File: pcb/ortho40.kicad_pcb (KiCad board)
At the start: 2 copper layers, 284 x 84 mm, 129 parts, among them J1 SWD, J2 USB_C_Receptacle_USB2.0, SW1 SW_Push, U1 RP2040, U2 XC6206PxxxMR, U3 W25Q128JVS, U4 USBLC6-2SC6, U5 ST7735S_1.8inch, Y1 12MHz

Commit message: Some net problems again ugh!
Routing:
- net GND: track 80.9 -> 92.2 mm
- net +3V3: track 113.9 -> 121.1 mm, vias 6 -> 8
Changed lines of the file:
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@@
   (segment (start 180 42) (end 182 40) (width 0.6) (layer "F.Cu") (net 1))
   (segment (start 172 55) (end 171 54) (width 0.381) (layer "F.Cu") (net 1))
+  (segment (start 177.602214 46.197786) (end 177.602214 49.324478) (width 0.2) (layer "F.Cu") (net 1))
+  (segment (start 179.4 44.4) (end 177.602214 46.197786) (width 0.2) (layer "F.Cu") (net 1))
   (segment (start 191 60) (end 191 64) (width 0.2) (layer "F.Cu") (net 1))
   (segment (start 174 57) (end 174 59) (width 0.381) (layer "F.Cu") (net 1))
@@
   (segment (start 191 52) (end 191 60) (width 0.2) (layer "F.Cu") (net 1))
   (via (at 189 66) (size 0.6) (drill 0.3) (layers "F.Cu" "B.Cu") (net 1))
+  (via (at 179.4 44.4) (size 0.6) (drill 0.3) (layers "F.Cu" "B.Cu") (net 1))
+  (via (at 177.602214 49.324478) (size 0.6) (drill 0.3) (layers "F.Cu" "B.Cu") (net 1))
   (via (at 185 39) (size 0.6) (drill 0.3) (layers "F.Cu" "B.Cu") (net 1))
   (via (at 190 51) (size 0.6) (drill 0.3) (layers "F.Cu" "B.Cu") (net 1))
@@
   (segment (start 177.4 46.5625) (end 177.4 45.88) (width 0.2) (layer "B.Cu") (net 1))
   (segment (start 172.52 37.4825) (end 172.52 37.48) (width 0.6) (layer "B.Cu") (net 1))
-  (segment (start 179.4 45.4) (end 179.4 43.6) (width 0.2) (layer "B.Cu") (net 1))
+  (segment (start 179.4 45.4) (end 179.4 44.4) (width 0.2) (layer "B.Cu") (net 1))
   (segment (start 188.321178 51) (end 190 51) (width 0.2) (layer "B.Cu") (net 1))
   (segment (start 179.4 46.5625) (end 179.4 46.030025) (width 0.2) (layer "B.Cu") (net 1))
@@
   (segment (start 170 54) (end 170 53.321178) (width 0.381) (layer "B.Cu") (net 1))
   (segment (start 179.4 46.5625) (end 179.4 46.696397) (width 0.2) (layer "B.Cu") (net 1))
-  (segment locked (start 179.8 47.096397) (end 180.075048 47.371445) (width 0.2) (layer "B.Cu") (net 1))
+  (segment (start 179.8 47.096441) (end 180.121434 47.417875) (width 0.2) (layer "B.Cu") (net 1))
+  (segment (start 177.382782 49.54391) (end 177.382782 51) (width 0.2) (layer "B.Cu") (net 1))
   (segment (start 171 51) (end 169.339411 52.660589) (width 0.2) (layer "B.Cu") (net 1))
   (segment (start 179.4 46.696397) (end 179.8 47.096397) (width 0.2) (layer "B.Cu") (net 1))
@@
   (segment (start 177.4 45.88) (end 175 43.48) (width 0.2) (layer "B.Cu") (net 1))
   (segment (start 177.8 47) (end 177.4 47.4) (width 0.2) (layer "B.Cu") (net 1))
-  (segment (start 177.382782 51) (end 177.645429 51.262647) (width 0.2) (layer "B.Cu") (net 1))
+  (segment (start 179.8 47.096397) (end 179.8 47.096441) (width 0.2) (layer "B.Cu") (net 1))
   (segment (start 176.5625 51) (end 171 51) (width 0.2) (layer "B.Cu") (net 1))
   (segment (start 172.51 65) (end 173 65) (width 0.381) (layer "B.Cu") (net 1))
@@
   (segment (start 174.43 59.43) (end 174.43 63.57) (width 0.381) (layer "B.Cu") (net 1))
   (segment (start 177.8 46.28) (end 177.4 45.88) (width 0.2) (layer "B.Cu") (net 1))
+  (segment (start 177.645429 49.367693) (end 177.602214 49.324478) (width 0.2) (layer "B.Cu") (net 1))
   (segment (start 183.4375 47.4) (end 182.582141 47.4) (width 0.2) (layer "B.Cu") (net 1))
+  (segment (start 179.4 44.4) (end 179.4 43.6) (width 0.2) (layer "B.Cu") (net 1))
   (segment (start 186 46.48) (end 185 46.48) (width 0.2) (layer "B.Cu") (net 1))
   (segment (start 177.4 46.5625) (end 177.4 47.4) (width 0.2) (layer "B.Cu") (net 1))
+  (segment (start 177.602214 49.324478) (end 177.382782 49.54391) (width 0.2) (layer "B.Cu") (net 1))
   (segment (start 179.6 45.6) (end 179.4 45.6) (width 0.2) (layer "B.Cu") (net 1))
   (segment (start 172.999309 43.96482) (end 172.999309 45.96482) (width 0.381) (layer "B.Cu") (net 1))
@@
   (segment (start 180 50) (end 180 48.725) (width 0.635) (layer "F.Cu") (net 2))
   (segment (start 180 51.275) (end 178.725 51.275) (width 0.635) (layer "F.Cu") (net 2))
-  (segment (start 181.275 50) (end 181.275 51.275) (width 0.635) (layer "F.Cu") (net 2))
   (segment (start 181.275 48.725) (end 181.275 50) (width 0.635) (layer "F.Cu") (net 2))
+  (segment (start 181.275 51.275) (end 181.275 50) (width 0.635) (layer "F.Cu") (net 2))
   (segment (start 181.275 48.725) (end 180 48.725) (width 0.635) (layer "F.Cu") (net 2))
   (segment (start 178.725 48.725) (end 178.725 50) (width 0.635) (layer "F.Cu") (net 2))
@@
   (segment (start 189.90178 32.02307) (end 189.90178 30.40322) (width 0.381) (layer "B.Cu") (net 2))
   (segment (start 181.876058 41.123942) (end 182.573112 41.123942) (width 0.381) (layer "B.Cu") (net 2))
+  (segment (start 184.32 23.13) (end 184.165 23.13) (width 0.2) (layer "B.Cu") (net 2))
   (segment (start 176.455282 42.540759) (end 175.540759 42.540759) (width 0.381) (layer "B.Cu") (net 2))
+  (segment (start 184.32 18.95) (end 184.32 23.13) (width 0.2) (layer "B.Cu") (net 2))
   (segment (start 181 29.660618) (end 181.660618 29) (width 0.381) (layer "B.Cu") (net 2))
   (segment (start 181 53.4375) (end 181 56.384314) (width 0.2) (layer "B.Cu") (net 2))
   (segment (start 177.156607 57.811617) (end 176.496018 58.472206) (width 0.381) (layer "B.Cu") (net 2))
   (segment (start 186 60.6905) (end 186 61.47) (width 0.381) (layer "B.Cu") (net 2))
+  (segment (start 175.835 23.13) (end 176.75 24.045) (width 0.2) (layer "B.Cu") (net 2))
   (segment (start 175.68 23.68) (end 176 24) (width 0.2) (layer "B.Cu") (net 2))
   (segment (start 189.90178 30.40322) (end 189.905 30.4) (width 0.381) (layer "B.Cu") (net 2))
@@
   (segment (start 184 26) (end 185 26) (width 0.381) (layer "B.Cu") (net 2))
   (segment (start 175 42) (end 175 41) (width 0.381) (layer "B.Cu") (net 2))
+  (segment (start 175.68 23.13) (end 175.68 19.32) (width 0.2) (layer "B.Cu") (net 2))
   (segment (start 181.5 42.02) (end 181.5 41.5) (width 0.381) (layer "B.Cu") (net 2))
   (segment (start 187.25 68.25) (end 187.25 76.5) (width 0.381) (layer "B.Cu") (net 2))
   (segment (start 175.44551 65.44551) (end 175.49471 65.44551) (width 0.381) (layer "B.Cu") (net 2))
+  (segment (start 175.68 19.32) (end 176 19) (width 0.2) (layer "B.Cu") (net 2))
   (segment (start 176 26) (end 176.75 25.25) (width 0.381) (layer "B.Cu") (net 2))
   (segment (start 180.27 63.43) (end 180.9 62.8) (width 0.25) (layer "B.Cu") (net 2))
@@
   (segment (start 175 42.52) (end 175 42) (width 0.381) (layer "B.Cu") (net 2))
   (segment (start 176.0125 36) (end 175.95 35.9375) (width 0.6) (layer "B.Cu") (net 2))
+  (segment (start 175.68 23.13) (end 175.835 23.13) (width 0.2) (layer "B.Cu") (net 2))
   (segment (start 178 63.43) (end 178 64.95) (width 0.25) (layer "B.Cu") (net 2))
   (segment (start 188.339411 52.339411) (end 189 53) (width 0.381) (layer "B.Cu") (net 2))
@@
   (segment (start 176.75 25.25) (end 176.75 24.045) (width 0.381) (layer "B.Cu") (net 2))
   (segment (start 181 56.384314) (end 182.165686 57.55) (width 0.2) (layer "B.Cu") (net 2))
+  (segment (start 184.165 23.13) (end 183.25 24.045) (width 0.2) (layer "B.Cu") (net 2))
   (segment (start 175 26) (end 176 26) (width 0.381) (layer "B.Cu") (net 2))
   (segment (start 178 36) (end 176.0125 36) (width 0.6) (layer "B.Cu") (net 2))
@@
   (segment (start 179.760618 29) (end 180.661024 29) (width 0.381) (layer "B.Cu") (net 3))
   (segment (start 179.760618 29) (end 178.360618 30.4) (width 0.381) (layer "B.Cu") (net 3))
+  (segment (start 180.188356 46.832225) (end 179.181588 47.838993) (width 0.2) (layer "F.Cu") (net 4))
   (segment (start 179.399059 52.328303) (end 179.399059 53.600941) (width 0.2) (layer "F.Cu") (net 4))
   (segment (start 179.382115 52.0995) (end 179.382115 52.311359) (width 0.2) (layer "F.Cu") (net 4))
+  (segment (start 179.181588 47.838993) (end 178.889817 47.838993) (width 0.2) (layer "F.Cu") (net 4))
   (segment (start 179.395412 55.901146) (end 178.824352 56.472206) (width 0.2) (layer "F.Cu") (net 4))
   (segment (start 178.824352 56.472206) (end 178.496018 56.472206) (width 0.2) (layer "F.Cu") (net 4))
+  (segment (start 180.536802 43.644915) (end 180.188356 43.993361) (width 0.2) (layer "F.Cu") (net 4))
+  (segment (start 180.188356 43.993361) (end 180.188356 46.832225) (width 0.2) (layer "F.Cu") (net 4))
   (segment (start 179.399059 53.600941) (end 179.395412 53.604588) (width 0.2) (layer "F.Cu") (net 4))
-  (segment (start 178.889817 47.838993) (end 180.536802 46.192008) (width 0.381) (layer "F.Cu") (net 4))
   (segment (start 179.395412 53.604588) (end 179.395412 55.901146) (width 0.2) (layer "F.Cu") (net 4))
-  (segment (start 180.536802 46.192008) (end 180.536802 43.644915) (width 0.381) (layer "F.Cu") (net 4))
   (segment (start 179.382115 52.311359) (end 179.399059 52.328303) (width 0.2) (layer "F.Cu") (net 4))
   (via (at 180.536802 43.644915) (size 0.6) (drill 0.3) (layers "F.Cu" "B.Cu") (net 4))
@@
         (xy 182.271341 52.167774)
         (xy 182.271341 47.767774)
-        (xy 179.471341 47.767774)
-        (xy 179.471341 47.567774)
+        (xy 179.235724 47.771418)
+        (xy 179.155959 47.655981)
         (xy 179.071341 47.567774)
         (xy 179.071341 47.167774)

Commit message: Add track just in case
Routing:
- net +3V3: track 121.1 -> 131.3 mm
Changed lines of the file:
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@@
     (grid_origin 174 43)
     (pcbplotparams
-      (layerselection 0x00010fc_ffffffff)
+      (layerselection 0x00010ec_ffffffff)
       (disableapertmacros false)
       (usegerberextensions false)
@@
   (segment (start 185 51) (end 187 51) (width 0.2) (layer "B.Cu") (net 1))
   (segment (start 172.52 38.985) (end 172.52 40) (width 0.6) (layer "B.Cu") (net 1))
-  (segment (start 179.8 53.4375) (end 179.8 52.899196) (width 0.2) (layer "B.Cu") (net 1))
   (segment (start 179.8 57.086077) (end 179.371503 57.514574) (width 0.2) (layer "B.Cu") (net 1))
   (segment (start 176.5625 51) (end 177.382782 51) (width 0.2) (layer "B.Cu") (net 1))
@@
   (segment (start 170 53.321178) (end 169.339411 52.660589) (width 0.381) (layer "B.Cu") (net 1))
   (segment (start 177.8 46.5625) (end 177.8 46.28) (width 0.2) (layer "B.Cu") (net 1))
+  (segment (start 180.121434 47.417875) (end 182.564266 47.417875) (width 0.2) (layer "B.Cu") (net 1))
   (segment (start 189.25 66.25) (end 189.25 76.5) (width 0.2) (layer "B.Cu") (net 1))
   (segment (start 187 51) (end 187.660589 51.660589) (width 0.2) (layer "B.Cu") (net 1))
@@
   (segment (start 172.52 37.4825) (end 172.52 38.985) (width 0.6) (layer "B.Cu") (net 1))
   (segment (start 177.8 46.5625) (end 177.8 47) (width 0.2) (layer "B.Cu") (net 1))
-  (segment (start 179.8 52.899196) (end 179.95765 52.741546) (width 0.2) (layer "B.Cu") (net 1))
+  (segment (start 179.8 53.4375) (end 179.8 52.899196) (width 0.2) (layer "B.Cu") (net 1))
   (segment (start 177.4 47.4) (end 176.5625 47.4) (width 0.2) (layer "B.Cu") (net 1))
   (segment (start 189 66) (end 189.25 66.25) (width 0.2) (layer "B.Cu") (net 1))
+  (segment (start 182.582141 47.4) (end 182.542926 47.439215) (width 0.2) (layer "B.Cu") (net 1))
   (segment (start 179.4 46.030025) (end 179.4 45.6) (width 0.2) (layer "B.Cu") (net 1))
   (segment (start 179.8 46.5625) (end 179.8 45.8) (width 0.2) (layer "B.Cu") (net 1))
@@
   (segment (start 183.4375 51) (end 182.624358 51) (width 0.2) (layer "B.Cu") (net 1))
   (segment (start 183.4375 51) (end 185 51) (width 0.2) (layer "B.Cu") (net 1))
+  (segment (start 179.8 52.899196) (end 180.211675 52.487521) (width 0.2) (layer "B.Cu") (net 1))
+  (segment (start 182.510782 51.113576) (end 182.624358 51) (width 0.2) (layer "B.Cu") (net 1))
   (segment (start 186.095 37.6) (end 186.095 37.905) (width 0.6) (layer "B.Cu") (net 1))
   (segment (start 179.4 46.5625) (end 179.4 46.696614) (width 0.2) (layer "B.Cu") (net 1))
@@
   (segment (start 179.4 46.5625) (end 179.4 46.030025) (width 0.2) (layer "B.Cu") (net 1))
   (segment (start 179.8 53.4375) (end 179.8 57.086077) (width 0.2) (layer "B.Cu") (net 1))
+  (segment (start 182.624358 51) (end 182.542926 50.918568) (width 0.2) (layer "B.Cu") (net 1))
+  (segment (start 182.564266 47.417875) (end 182.582141 47.4) (width 0.2) (layer "B.Cu") (net 1))
   (segment (start 174.434489 47.4) (end 172.999309 45.96482) (width 0.2) (layer "B.Cu") (net 1))
   (segment (start 170 54) (end 170 53.321178) (width 0.381) (layer "B.Cu") (net 1))
@@
   (segment (start 174 43.48) (end 175 43.48) (width 0.6) (layer "B.Cu") (net 1))
   (segment (start 179.4 43.6) (end 179 43.2) (width 0.2) (layer "B.Cu") (net 1))
+  (segment (start 182.510782 52.184193) (end 182.510782 51.113576) (width 0.2) (layer "B.Cu") (net 1))
   (segment (start 177.4 45.88) (end 175 43.48) (width 0.2) (layer "B.Cu") (net 1))
   (segment (start 177.8 47) (end 177.4 47.4) (width 0.2) (layer "B.Cu") (net 1))
@@
   (segment (start 174 59) (end 174.43 59.43) (width 0.381) (layer "B.Cu") (net 1))
   (segment (start 173 65) (end 174.43 63.57) (width 0.381) (layer "B.Cu") (net 1))
+  (segment (start 182.542926 50.918568) (end 182.542926 47.439215) (width 0.2) (layer "B.Cu") (net 1))
   (segment (start 174.43 59.43) (end 174.43 63.57) (width 0.381) (layer "B.Cu") (net 1))
   (segment (start 177.8 46.28) (end 177.4 45.88) (width 0.2) (layer "B.Cu") (net 1))
@@
   (segment (start 179.4 44.4) (end 179.4 43.6) (width 0.2) (layer "B.Cu") (net 1))
   (segment (start 186 46.48) (end 185 46.48) (width 0.2) (layer "B.Cu") (net 1))
+  (segment (start 182.207454 52.487521) (end 182.510782 52.184193) (width 0.2) (layer "B.Cu") (net 1))
   (segment (start 177.4 46.5625) (end 177.4 47.4) (width 0.2) (layer "B.Cu") (net 1))
   (segment (start 177.602214 49.324478) (end 177.382782 49.54391) (width 0.2) (layer "B.Cu") (net 1))
   (segment (start 179.6 45.6) (end 179.4 45.6) (width 0.2) (layer "B.Cu") (net 1))
   (segment (start 172.999309 43.96482) (end 172.999309 45.96482) (width 0.381) (layer "B.Cu") (net 1))
+  (segment (start 180.211675 52.487521) (end 182.207454 52.487521) (width 0.2) (layer "B.Cu") (net 1))
   (segment (start 172.52 40) (end 172.52 42) (width 0.6) (layer "B.Cu") (net 1))
   (segment (start 178.725 48.725) (end 180 48.725) (width 0.635) (layer "F.Cu") (net 2))
@@
         (xy 179.071341 52.367774)
         (xy 179.871341 52.367774)
-        (xy 179.871341 52.167774)
-        (xy 182.271341 52.167774)
-        (xy 182.271341 47.767774)
+        (xy 179.871341 52)
+        (xy 182 52)
+        (xy 182 47.76597)
         (xy 179.235724 47.771418)
         (xy 179.155959 47.655981)

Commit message: Updates...
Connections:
- U1 pad 18: unconnected-(U1-Pad18) -> LCD_BACKLT
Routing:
- net LCD_BACKLT: track 0.00 -> 38.1 mm, vias 0 -> 2

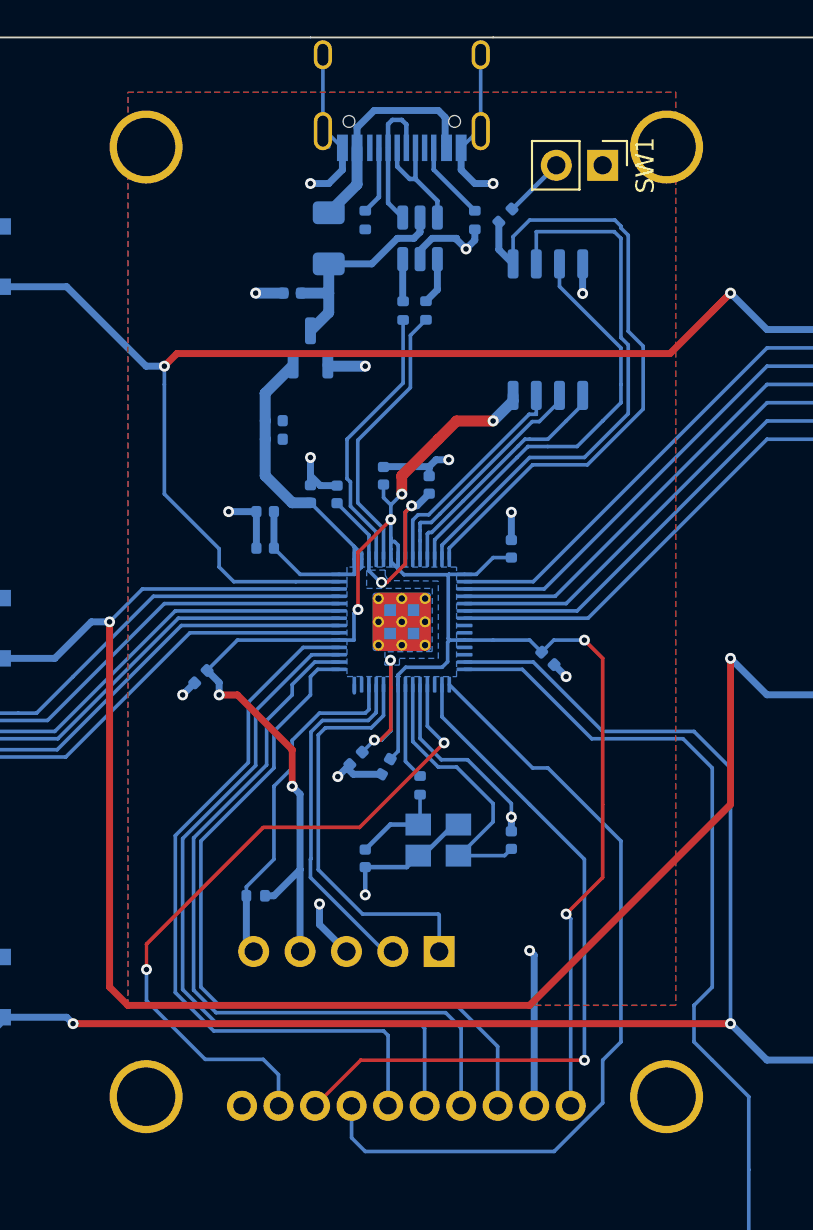
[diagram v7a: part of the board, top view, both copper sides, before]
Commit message: Update Display footprint
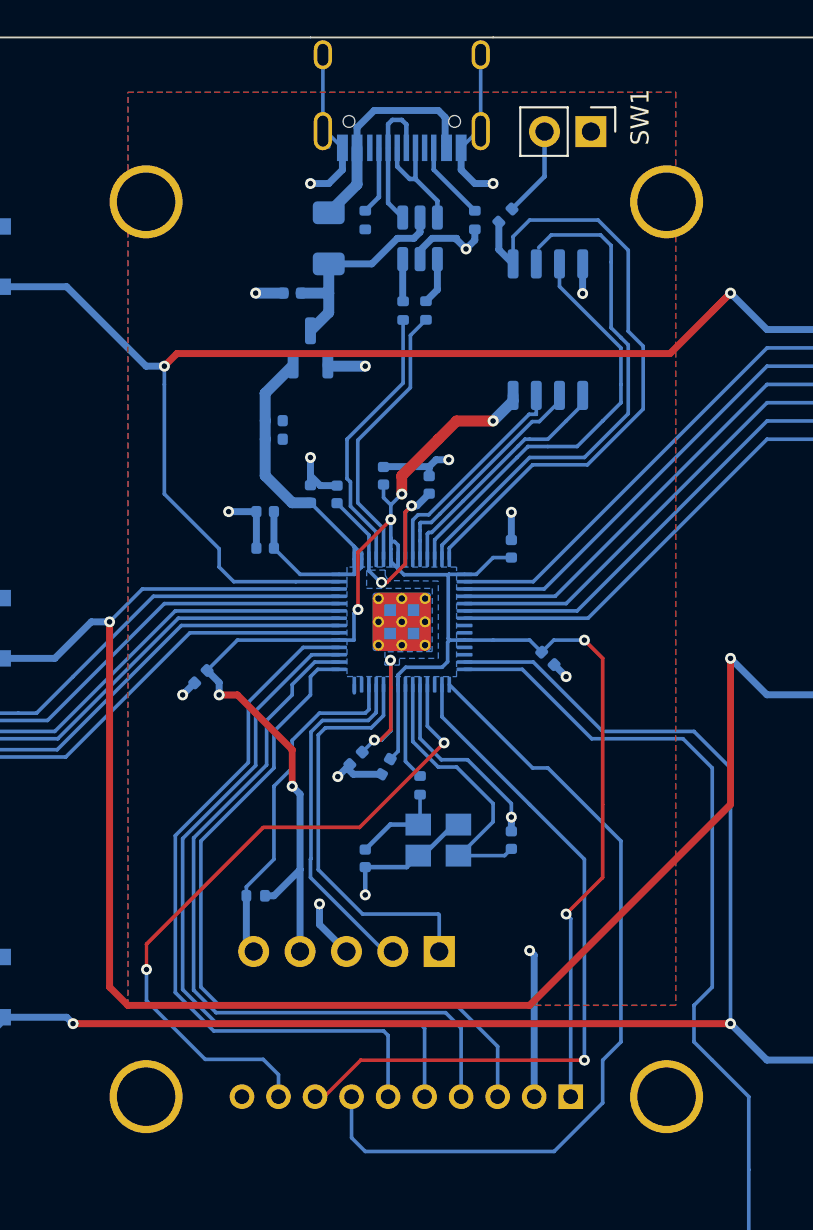
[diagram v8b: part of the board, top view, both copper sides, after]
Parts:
- moved SW1 1.95 mm to (190.4, 23.2)
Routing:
- net QSPI_SD1: track 30.3 -> 28.0 mm
- net /~{BOOTSEL}: track 3.42 -> 5.01 mm
- net QSPI_SS: track 35.4 -> 34.9 mm
